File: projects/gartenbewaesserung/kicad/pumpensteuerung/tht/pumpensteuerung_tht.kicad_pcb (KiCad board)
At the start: 2 copper layers, 100 x 85 mm, 26 parts, among them J1 Screw_Terminal_01x03, J2 Screw_Terminal_01x02, J3 I2C Terminal, J4 Screw_Terminal_01x03, J5 Screw_Terminal_01x03, K2 SANYOU_SRD_Form_C, K3 SANYOU_SRD_Form_C, K4 SANYOU_SRD_Form_C, Q1 S8050, Q2 S8050, Q3 S8050

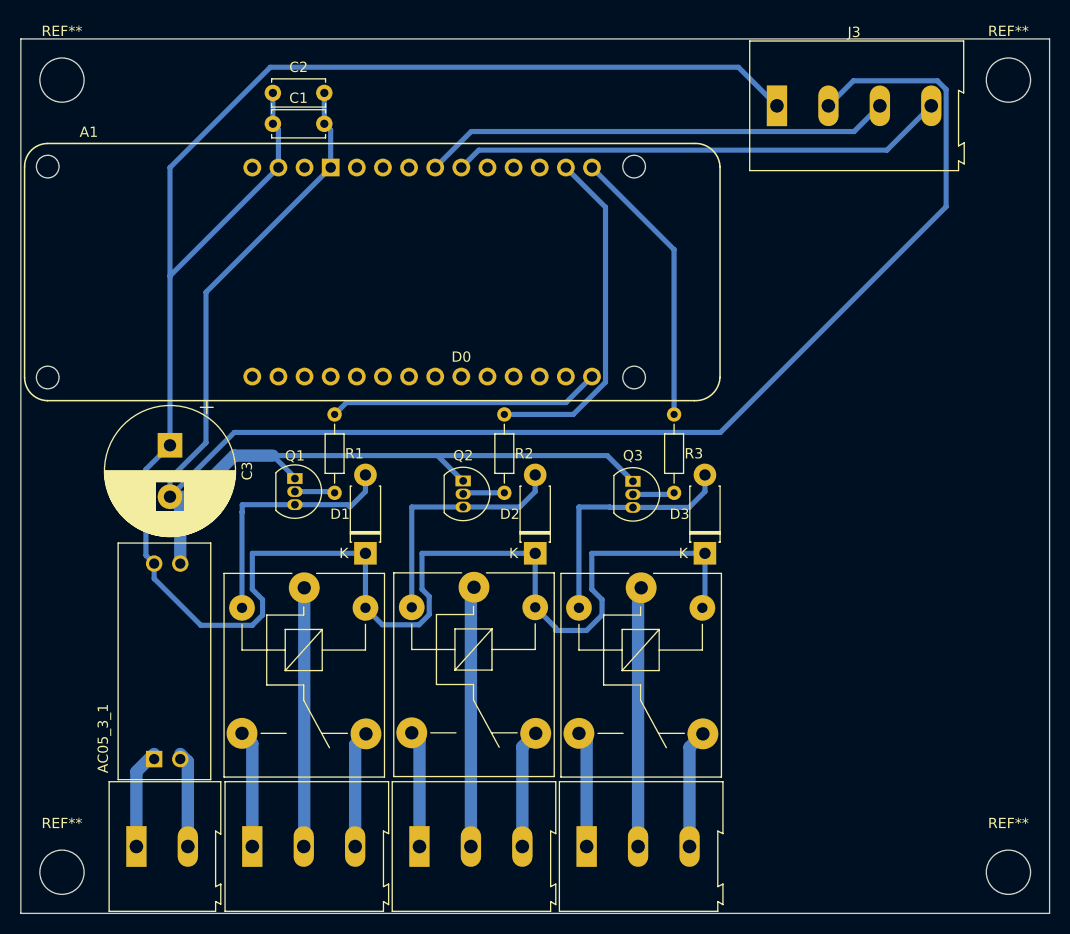
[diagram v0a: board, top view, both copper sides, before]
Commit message: [gartenbewaesserung(pcb)] fix some issue in pcb
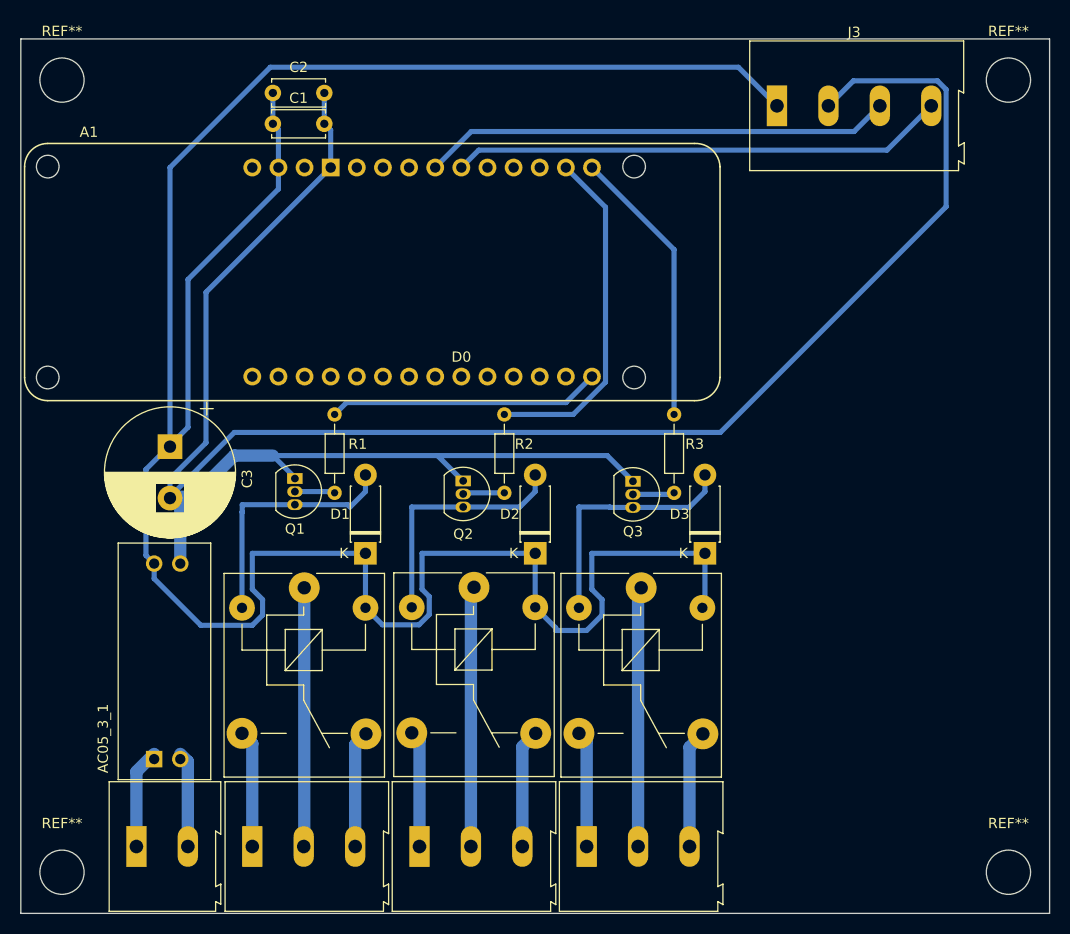
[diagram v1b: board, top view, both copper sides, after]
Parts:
- moved C3 0.13 mm to (65.0, 88.6)
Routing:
- net /+5V: track 224.6 -> 241.3 mm

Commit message: [gartenbewaesserung(pcb)] replace fake footprints with real one
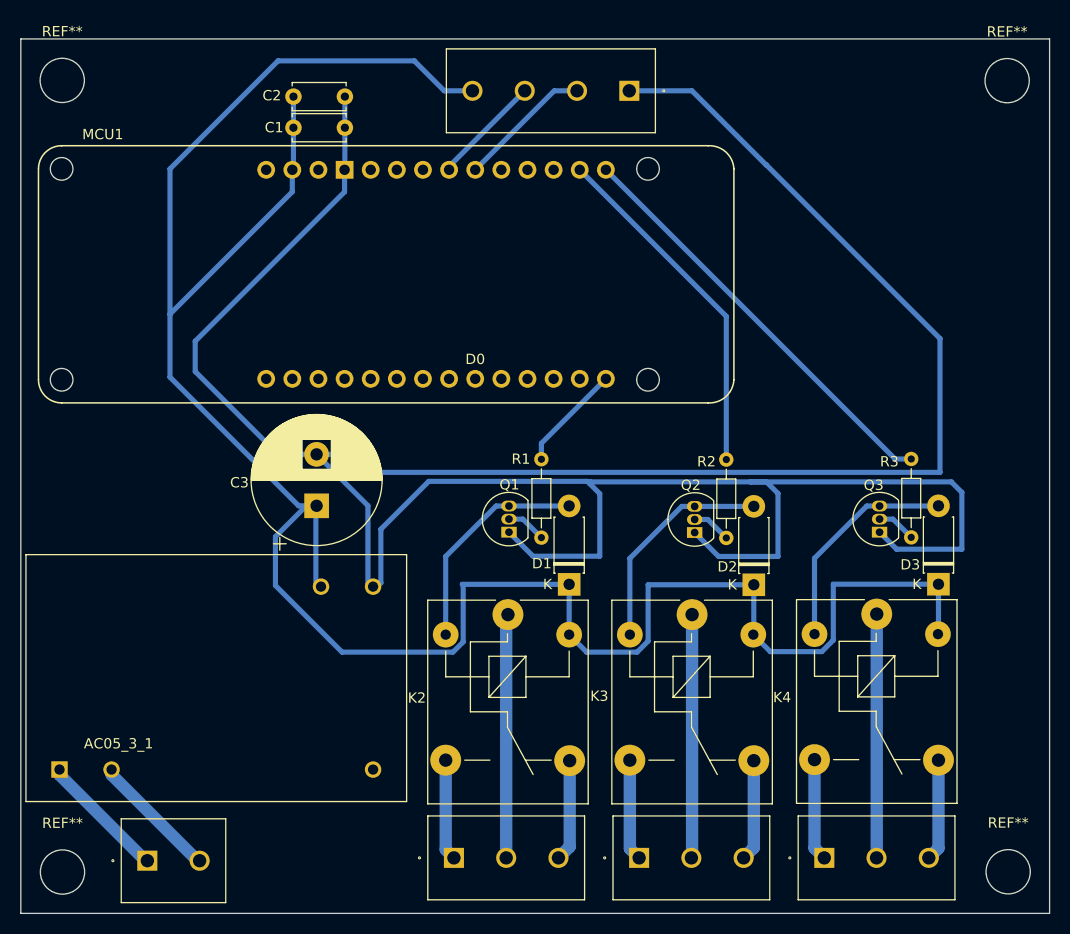
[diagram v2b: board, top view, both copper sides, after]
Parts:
- removed A1: Arduino_MKR_WAN_1310_Socket, PCM_arduino-library:Arduino_MKR_FOX_1200_Socket
- removed the REF** at (54.5, 53.0)
- removed the REF** at (146.5, 53.0)
- removed the REF** at (146.5, 130.0)
- removed the REF** at (54.5, 130.0)
- added MCU1: Arduino_MKR_WAN_1310_Socket, PCM_arduino-library:Arduino_MKR_FOX_1200_Socket, F.Cu at (54.5, 61.6)
- added REF**: MountingHole_4.3mm_M4_DIN965, MountingHole:MountingHole_4.3mm_M4_DIN965, F.Cu at (146.4, 53.1)
- added REF**: MountingHole_4.3mm_M4_DIN965, MountingHole:MountingHole_4.3mm_M4_DIN965, F.Cu at (54.5, 130.0)
- added REF**: MountingHole_4.3mm_M4_DIN965, MountingHole:MountingHole_4.3mm_M4_DIN965, F.Cu at (54.5, 53.0)
- added REF**: MountingHole_4.3mm_M4_DIN965, MountingHole:MountingHole_4.3mm_M4_DIN965, F.Cu at (146.5, 130.0)
- J1, J4, J5: footprint TerminalBlock:TerminalBlock_Altech_AK300-3_P5.00mm -> PhoenixContact:MKDSN 1,5_3-5,08
- J2: footprint TerminalBlock:TerminalBlock_Altech_AK300-2_P5.00mm -> PhoenixContact:MKDSN 1,5_2-5,08
- J3: footprint TerminalBlock:TerminalBlock_Altech_AK300-4_P5.00mm -> PhoenixContact:MKDSN 1,5_4-5,08
- moved Q3 24.5 mm to (134.0, 96.9), turned to 90 degrees
- moved R3 23.5 mm to (137.1, 89.8)
- moved J5 23.1 mm to (128.6, 128.6)
- moved Q2 23.1 mm to (116.0, 97.0), turned to 90 degrees
- moved K4 23.0 mm to (133.7, 104.9)
- moved D3 22.9 mm to (139.7, 102.0)
- moved R2 22.0 mm to (119.1, 89.9)
- moved D2 21.5 mm to (121.8, 102.1)
- moved Q1 21.5 mm to (98.0, 96.9), turned to 90 degrees
- moved J4 21.4 mm to (110.6, 128.6)
- moved K3 21.4 mm to (115.8, 105.0)
- moved R1 20.6 mm to (101.1, 89.9)
- moved D1 20.0 mm to (103.8, 102.0)
- moved K2 20.0 mm to (97.8, 105.0)
- moved J1 19.6 mm to (92.6, 128.6)
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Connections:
- J3 pad 1: /+5V -> /-5V
- J3 pad 2: /-5V -> /SDA
- J3 pad 4: /SDA -> /+5V
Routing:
- net /-5V: track 219.3 -> 292.6 mm
- net /SCL: track 45.8 -> 10.7 mm
- net /SDA: track 48.2 -> 13.2 mm
- net /+5V: track 241.3 -> 220.1 mm
- net /Hauptrelais: track 26.5 -> 10.4 mm
- net /Poolrelais: track 27.3 -> 41.3 mm
- net Net-(D1-A): track 26.2 -> 21.6 mm
- net GND: track 9.30 -> 12.5 mm
- net Net-(D3-A): track 24.3 -> 21.5 mm
- net VCC: track 9.71 -> 12.5 mm
- net Net-(D2-A): track 24.1 -> 21.6 mm
- net /Bewaesserungsrelais/NO: track 11.5 -> 9.86 mm
- net /Bewaesserungsrelais/IN: track 25.3 -> 23.7 mm
- net /Poolrelais/NO: track 11.5 -> 9.89 mm
- net /Hauptrelais/ON: track 11.4 -> 9.83 mm
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
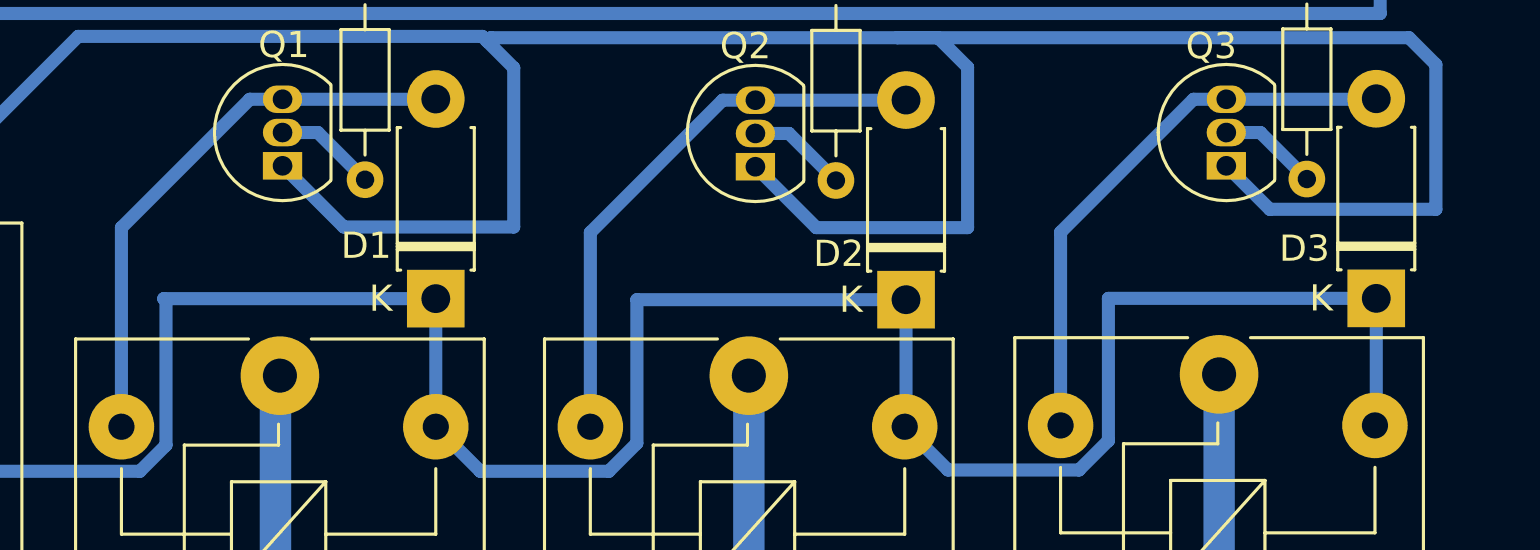
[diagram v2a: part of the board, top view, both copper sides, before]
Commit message: [gartenbewaesserung(pcb)] increase gap between high and low voltage
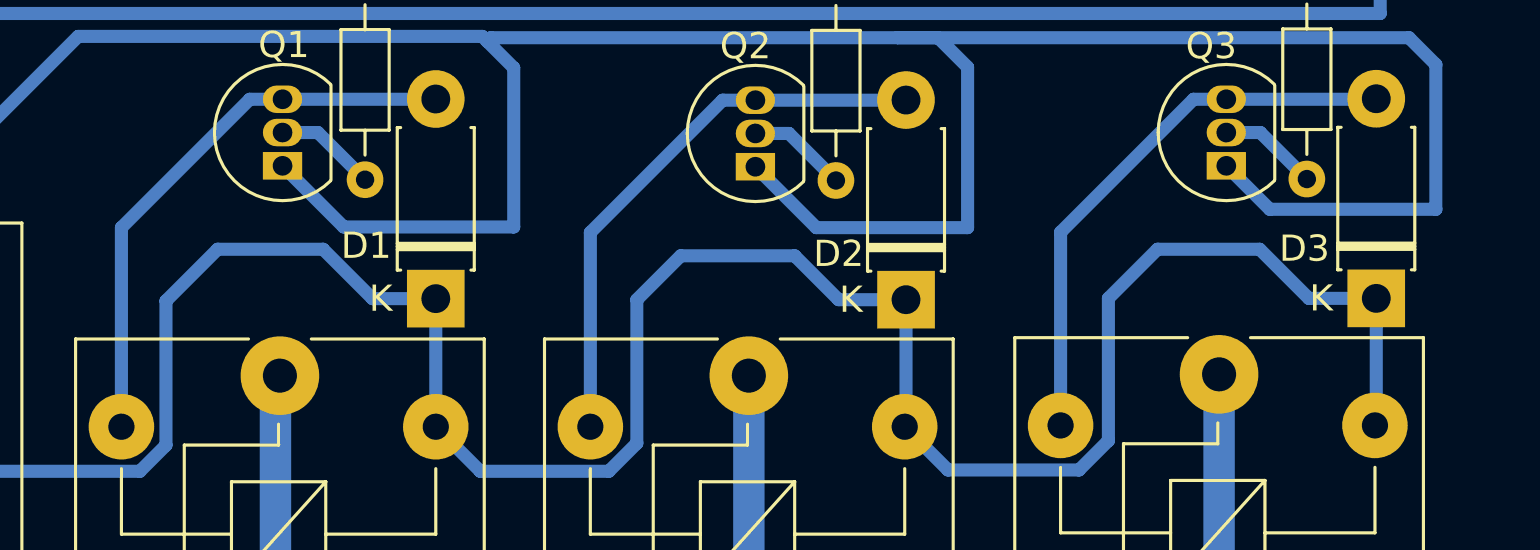
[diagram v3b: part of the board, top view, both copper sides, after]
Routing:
- net /+5V: track 220.1 -> 224.5 mm
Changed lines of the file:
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@@
 		)
 		(embedded_fonts no)
-		(model "/home/sebastian/workspaces/oss/3d-models/projects/gartenbewaesserung/kicad/libraries/footprints/AZFootprints.pretty/Mininetzteil.STEP"
+		(model "Mininetzteil.STEP"
 			(offset
 				(xyz 2.5 37.5 4.5)
@@
 	)
 	(segment
+		(start 92.504578 108.606)
+		(end 81.726 108.606)
+		(width 0.5)
+		(layer "B.Cu")
+		(net 4)
+	)
+	(segment
+		(start 78.25 94.38)
+		(end 79.25 94.38)
+		(width 0.5)
+		(layer "B.Cu")
+		(net 4)
+	)
+	(segment
 		(start 111.475 102.055)
 		(end 111.475 107.535578)
@@
 	)
 	(segment
-		(start 92.504578 108.606)
-		(end 81.726 108.606)
-		(width 0.5)
-		(layer "B.Cu")
-		(net 4)
-	)
-	(segment
-		(start 121.75 102.055)
-		(end 111.475 102.055)
-		(width 0.5)
-		(layer "B.Cu")
-		(net 4)
-	)
-	(segment
-		(start 78.25 94.38)
+		(start 117.5 100.38)
+		(end 113.15 100.38)
+		(width 0.5)
+		(layer "B.Cu")
+		(net 4)
+	)
+	(segment
+		(start 129.475 102.005)
+		(end 129.475 107.435578)
+		(width 0.5)
+		(layer "B.Cu")
+		(net 4)
+	)
+	(segment
+		(start 110.404578 108.606)
+		(end 105.501 108.606)
+		(width 0.5)
+		(layer "B.Cu")
+		(net 4)
+	)
+	(segment
+		(start 79.18 94.45)
 		(end 79.25 94.38)
 		(width 0.5)
@@
 	)
 	(segment
-		(start 79.18 94.45)
-		(end 79.25 94.38)
-		(width 0.5)
-		(layer "B.Cu")
-		(net 4)
-	)
-	(segment
 		(start 81.726 108.606)
 		(end 75.25 102.13)
@@
 	)
 	(segment
-		(start 103.8 102.015)
-		(end 93.415 102.015)
-		(width 0.5)
-		(layer "B.Cu")
-		(net 4)
-	)
-	(segment
 		(start 65 81.88)
 		(end 65 75.75)
@@
 	)
 	(segment
+		(start 95.472 100.13)
+		(end 93.501 102.101)
+		(width 0.5)
+		(layer "B.Cu")
+		(net 4)
+	)
+	(segment
+		(start 75.5 51.13)
+		(end 65 61.63)
+		(width 0.5)
+		(layer "B.Cu")
+		(net 4)
+	)
+	(segment
+		(start 93.501 107.609578)
+		(end 92.504578 108.606)
+		(width 0.5)
+		(layer "B.Cu")
+		(net 4)
+	)
+	(segment
+		(start 79.68 102.24)
+		(end 79.43 102.24)
+		(width 0.5)
+		(layer "B.Cu")
+		(net 4)
+	)
+	(segment
+		(start 93.501 102.101)
+		(end 93.501 107.609578)
+		(width 0.5)
+		(layer "B.Cu")
+		(net 4)
+	)
+	(segment
+		(start 121.75 106.855)
+		(end 121.7 106.905)
+		(width 0.5)
+		(layer "B.Cu")
+		(net 4)
+	)
+	(segment
+		(start 113.15 100.38)
+		(end 111.475 102.055)
+		(width 0.5)
+		(layer "B.Cu")
+		(net 4)
+	)
+	(segment
+		(start 119.175 102.055)
+		(end 117.5 100.38)
+		(width 0.5)
+		(layer "B.Cu")
+		(net 4)
+	)
+	(segment
+		(start 77 57.63)
+		(end 77 61.61)
+		(width 0.5)
+		(layer "B.Cu")
+		(net 4)
+	)
+	(segment
 		(start 111.475 107.535578)
 		(end 110.404578 108.606)
@@
 	)
 	(segment
-		(start 75.5 51.13)
-		(end 65 61.63)
-		(width 0.5)
-		(layer "B.Cu")
-		(net 4)
-	)
-	(segment
-		(start 93.501 107.609578)
-		(end 92.504578 108.606)
-		(width 0.5)
-		(layer "B.Cu")
-		(net 4)
-	)
-	(segment
-		(start 79.68 102.24)
-		(end 79.43 102.24)
-		(width 0.5)
-		(layer "B.Cu")
-		(net 4)
-	)
-	(segment
-		(start 110.404578 108.606)
-		(end 105.501 108.606)
-		(width 0.5)
-		(layer "B.Cu")
-		(net 4)
-	)
-	(segment
-		(start 93.501 102.101)
-		(end 93.501 107.609578)
+		(start 79.25 94.38)
+		(end 77.5 94.38)
+		(width 0.5)
+		(layer "B.Cu")
+		(net 4)
+	)
+	(segment
+		(start 99.5 100.13)
+		(end 95.472 100.13)
+		(width 0.5)
+		(layer "B.Cu")
+		(net 4)
+	)
+	(segment
+		(start 65 75.75)
+		(end 76.89 63.86)
+		(width 0.5)
+		(layer "B.Cu")
+		(net 4)
+	)
+	(segment
+		(start 75.25 97.38)
+		(end 78.25 94.38)
+		(width 0.5)
+		(layer "B.Cu")
+		(net 4)
+	)
+	(segment
+		(start 75.25 102.13)
+		(end 75.25 97.38)
+		(width 0.5)
+		(layer "B.Cu")
+		(net 4)
+	)
+	(segment
+		(start 121.75 102.055)
+		(end 119.175 102.055)
+		(width 0.5)
+		(layer "B.Cu")
+		(net 4)
+	)
+	(segment
+		(start 131.35 100.13)
+		(end 129.475 102.005)
 		(width 0.5)
 		(layer "B.Cu")
@@
 	)
 	(segment
-		(start 121.75 106.855)
-		(end 121.7 106.905)
-		(width 0.5)
-		(layer "B.Cu")
-		(net 4)
-	)
-	(segment
-		(start 77 57.63)
-		(end 77 61.61)
-		(width 0.5)
-		(layer "B.Cu")
-		(net 4)
-	)
-	(segment
-		(start 79.25 94.38)
-		(end 77.5 94.38)
-		(width 0.5)
-		(layer "B.Cu")
-		(net 4)
-	)
-	(segment
-		(start 65 75.75)
-		(end 76.89 63.86)
-		(width 0.5)
-		(layer "B.Cu")
-		(net 4)
-	)
-	(segment
-		(start 75.25 97.38)
-		(end 78.25 94.38)
-		(width 0.5)
-		(layer "B.Cu")
-		(net 4)
-	)
-	(segment
-		(start 75.25 102.13)
-		(end 75.25 97.38)
-		(width 0.5)
-		(layer "B.Cu")
-		(net 4)
-	)
-	(segment
-		(start 93.415 102.015)
-		(end 93.501 102.101)
+		(start 105.501 108.606)
+		(end 103.8 106.905)
 		(width 0.5)
 		(layer "B.Cu")
@@
 	)
 	(segment
-		(start 129.475 102.005)
-		(end 129.475 107.435578)
-		(width 0.5)
-		(layer "B.Cu")
-		(net 4)
-	)
-	(segment
 		(start 139.7 102.005)
 		(end 139.7 106.805)
@@
 	)
 	(segment
+		(start 139.7 102.005)
+		(end 137.125 102.005)
+		(width 0.5)
+		(layer "B.Cu")
+		(net 4)
+	)
+	(segment
 		(start 65 61.63)
 		(end 65 75.75)
@@
 	)
 	(segment
-		(start 139.7 102.005)
-		(end 129.475 102.005)
+		(start 103.8 102.015)
+		(end 101.385 102.015)
+		(width 0.5)
+		(layer "B.Cu")
+		(net 4)
+	)
+	(segment
+		(start 135.25 100.13)
+		(end 131.35 100.13)
 		(width 0.5)
 		(layer "B.Cu")
@@
 	)
 	(segment
-		(start 105.501 108.606)
-		(end 103.8 106.905)
-		(width 0.5)
-		(layer "B.Cu")
+		(start 101.385 102.015)
+		(end 99.5 100.13)
+		(width 0.5)
+		(layer "B.Cu")
+		(net 4)
+	)
+	(segment
+		(start 137.125 102.005)
+		(end 135.25 100.13)
+		(width 0.5)
+		(layer "B.Cu")

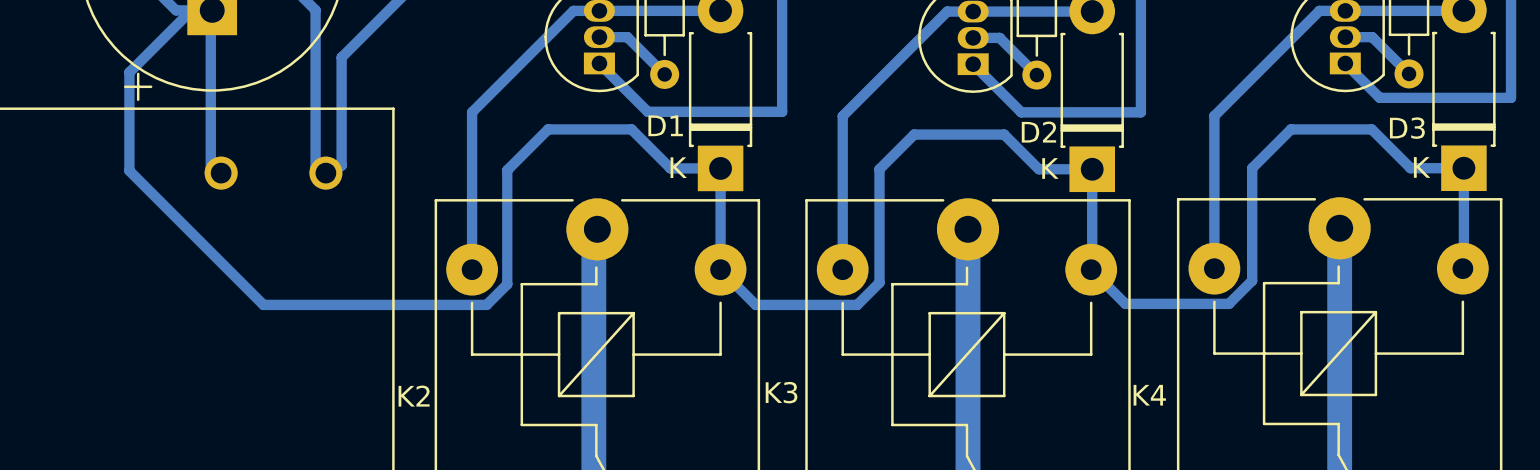
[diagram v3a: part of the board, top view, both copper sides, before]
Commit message: [gartenbewaesserung(pcb)] 'airgap' between high voltage and low voltage
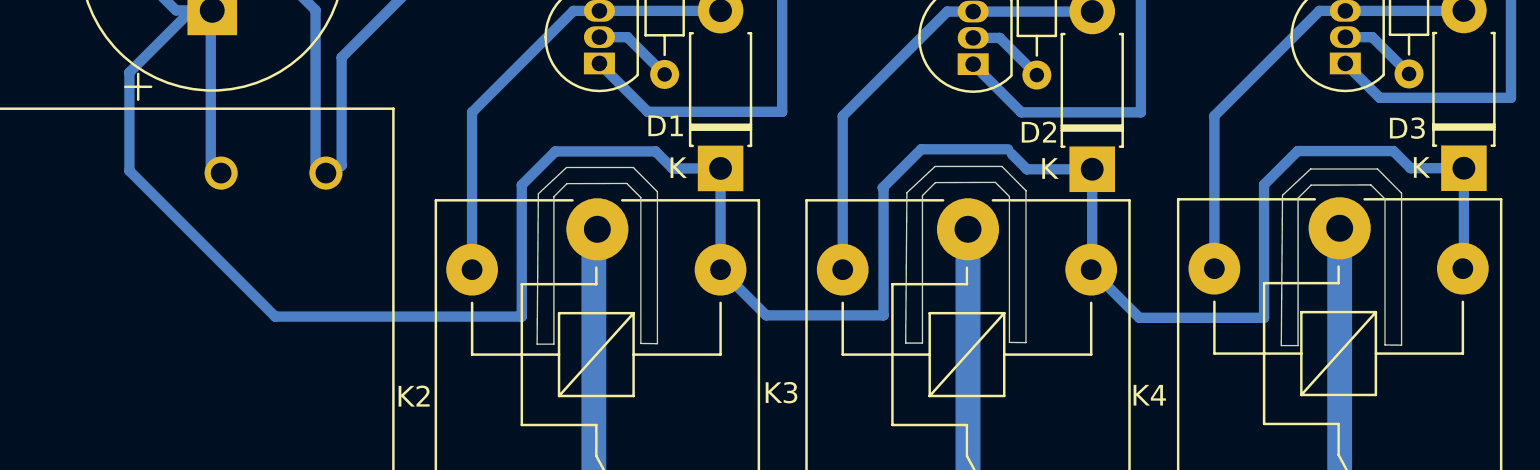
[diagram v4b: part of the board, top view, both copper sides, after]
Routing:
- net /+5V: track 224.5 -> 226.0 mm
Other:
- outline, holes or cut-outs redrawn
